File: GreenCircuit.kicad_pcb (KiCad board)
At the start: 2 copper layers, 114.9 x 97.8 mm, 71 parts, among them J1 AVR ISP 6, J2 USB_A-Connector, SW1 SW_Push, SW10 SW_Push, SW11 SW_Push, SW12 SW_Push, SW13 SW_Push, SW14 SW_Push, SW15 SW_Push, SW16 SW_Push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

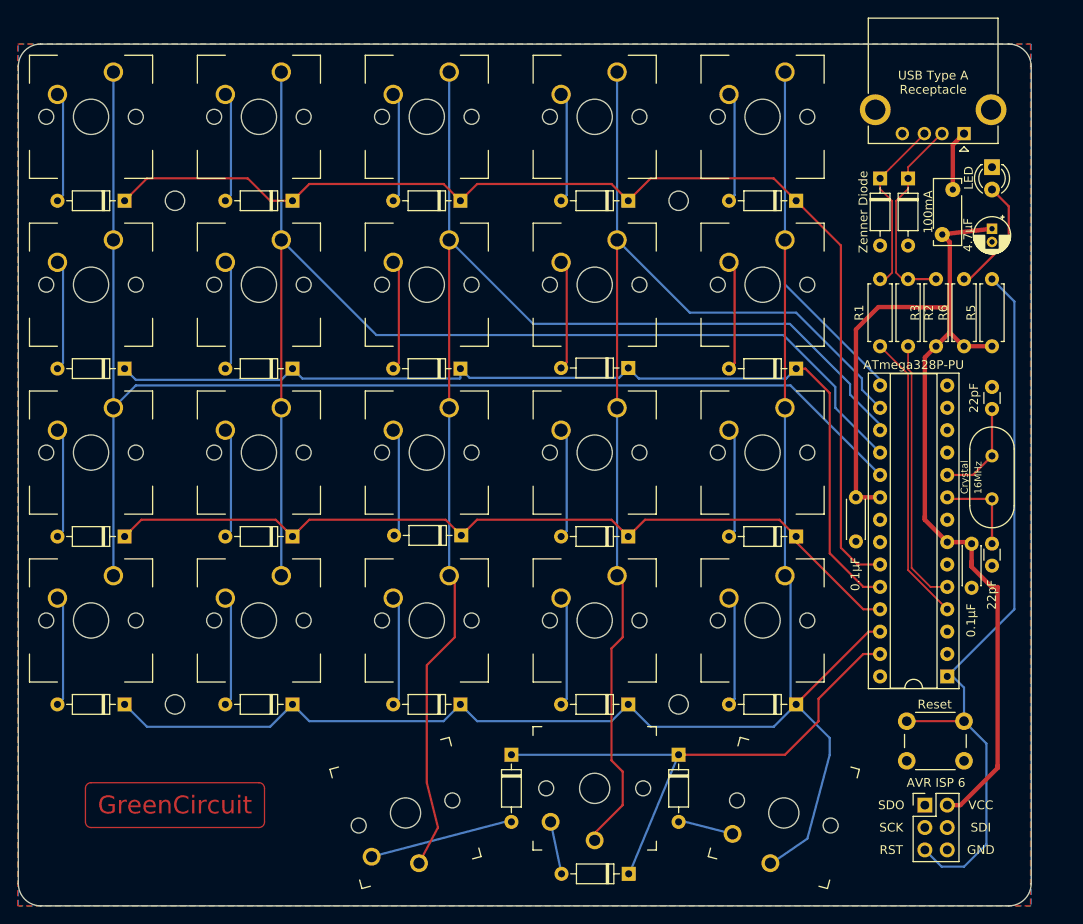
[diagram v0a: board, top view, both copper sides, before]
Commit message: isp reroute
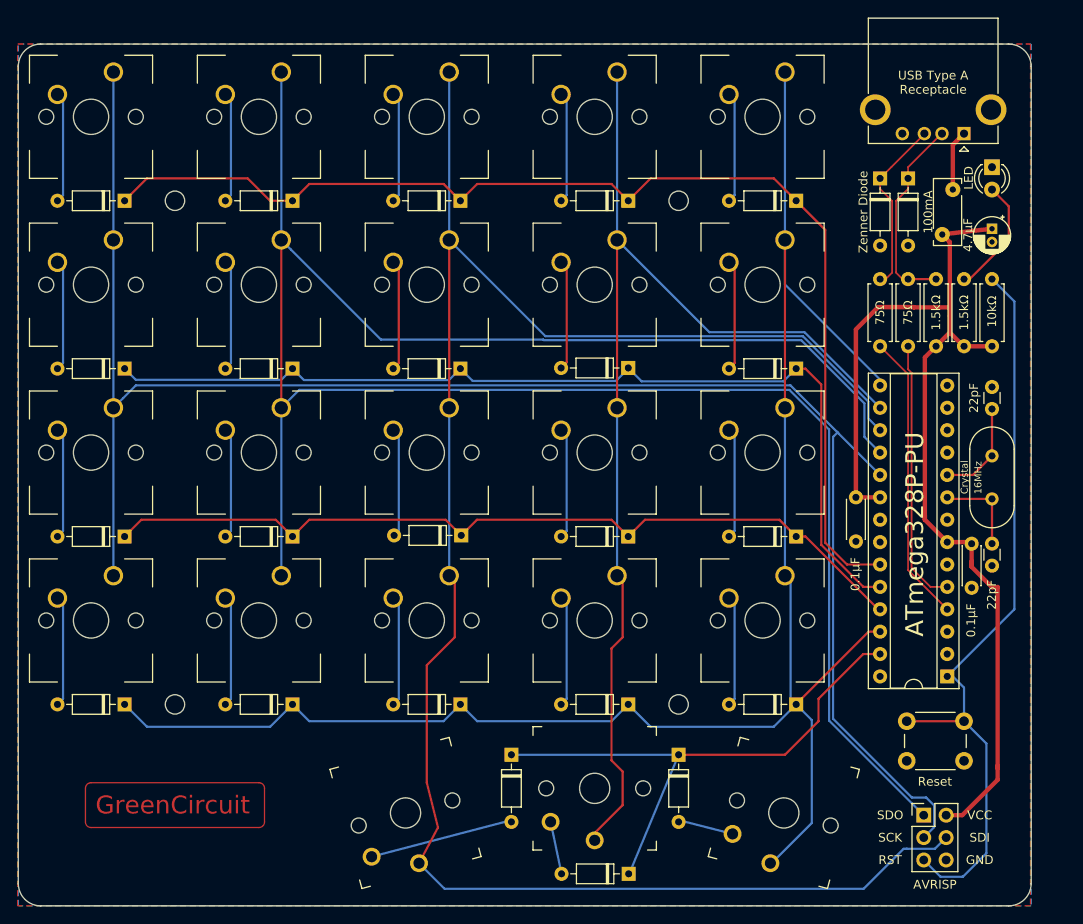
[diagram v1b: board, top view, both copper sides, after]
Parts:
- J1: value AVR ISP 6 -> AVRISP
- moved J1 1.15 mm to (179.8, 145.7)
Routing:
- net Col1: track 137.1 -> 251.0 mm
- net Col2: track 151.1 -> 214.6 mm
- net Col0: track 149.4 -> 201.9 mm
- net Col4: track 211.8 -> 210.4 mm
- net +5V: track 120.9 -> 122.3 mm
- net Reset: track 85.9 -> 87.2 mm
- net Col3: track 128.3 -> 127.5 mm
- net Row0: track 130.3 -> 131.0 mm
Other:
- board text added: "Rev 0.4 Oct 2020 James Sa"
- board text removed: "Rev 0.3 Sep 2020 James Sa"

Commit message: add indicative LED
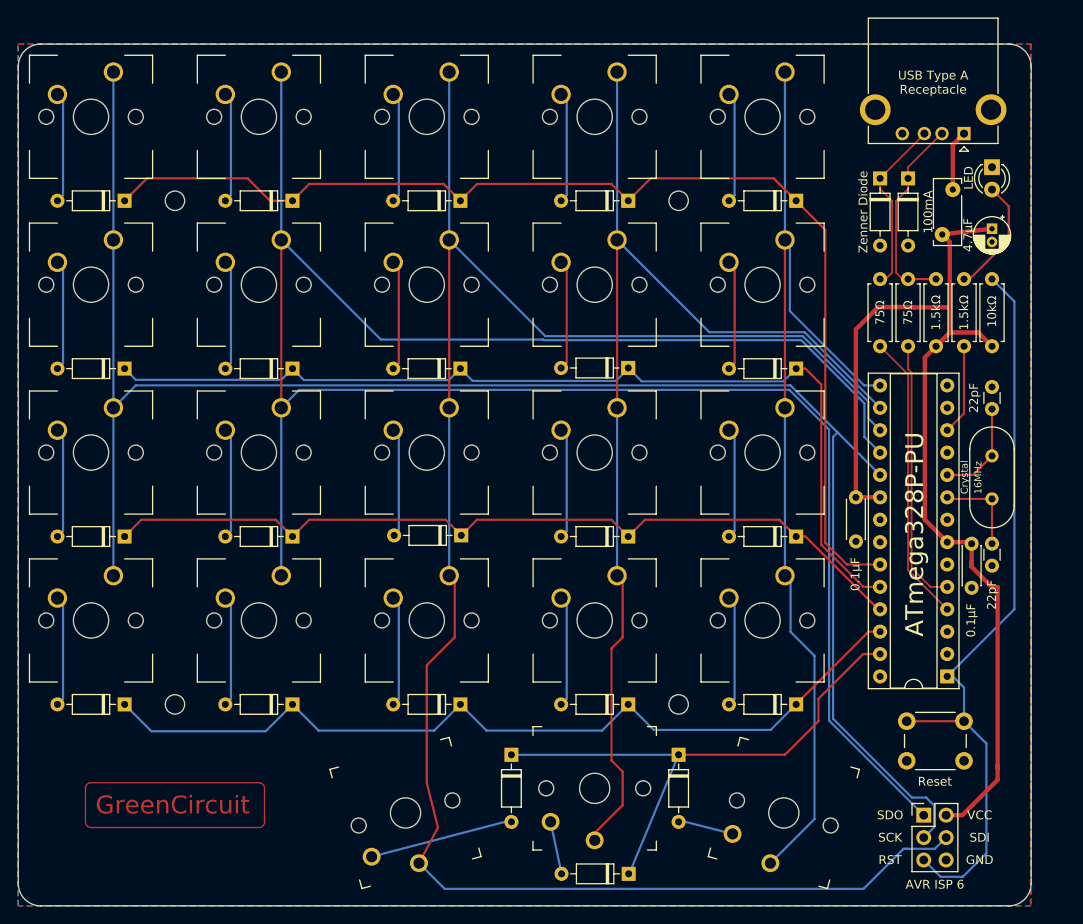
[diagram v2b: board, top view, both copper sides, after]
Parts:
- J1: value AVRISP -> AVR ISP 6
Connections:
- D16 pad 1: Col4 -> Row3
- D17 pad 1: Col4 -> Row3
- D18 pad 1: Col4 -> Row3
- D19 pad 1: Col4 -> Row3
- D20 pad 1: Col4 -> Row3
- R6 pad 1: +5V -> Net-(R6-Pad1)
- U1 pad 12: (no net) -> Net-(R6-Pad1)
- U1 pad 26: Col4 -> Row3
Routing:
- net Row3: track 0.00 -> 99.0 mm
- net Col4: track 210.4 -> 115.5 mm
- net Net-(R6-Pad1): track 0.00 -> 10.4 mm

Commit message: 220ohm for LED
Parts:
- R6: value 1.5kΩ -> 220Ω
- moved R5 3.17 mm to (184.4, 92.5)
- moved R6 3.17 mm to (187.5, 92.5)
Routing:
- net +5V: track 122.3 -> 119.1 mm
- net Net-(R6-Pad1): track 10.4 -> 11.6 mm
- net Net-(D26-Pad2): track 13.4 -> 12.3 mm
- net Reset: track 87.2 -> 88.1 mm

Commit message: v0.5
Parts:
- removed the J2 at (184.4, 68.4)
- removed Logo_KiCad: KiCad-Logo_20mm_SilkScreen, Symbol:KiCad-Logo_20mm_SilkScreen
- removed OSHW_Logo: OSHW-Logo2_36.5x30mm_SilkScreen, Symbol:OSHW-Logo2_36.5x30mm_SilkScreen
- added Mini USB: USB_B_Mini, digikey-footprints:USB_Mini_B_Female_548190519, F.Cu at (182.5, 66.5)
- J2: renamed from J1; value AVR ISP 6 -> AVR ISP
- moved D23 32.1 mm to (183.6, 144.2), turned to 255 degrees
- moved D22 20.3 mm to (161.5, 138.9), turned to 270 degrees
- moved H3 19.1 mm to (94.8, 114.1)
- moved D18 14.5 mm to (132.9, 119.8), turned to 270 degrees
- moved D3 14.5 mm to (132.9, 62.7), turned to 270 degrees
- moved D8 14.5 mm to (132.9, 81.7), turned to 270 degrees
- moved D1 14.5 mm to (94.8, 62.7), turned to 270 degrees
- moved D10 14.5 mm to (171.0, 81.7), turned to 270 degrees
- moved D16 14.5 mm to (94.8, 119.8), turned to 270 degrees
- moved D17 14.5 mm to (113.9, 119.8), turned to 270 degrees
- moved D19 14.5 mm to (152.0, 119.8), turned to 270 degrees
- moved D2 14.5 mm to (113.9, 62.7), turned to 270 degrees
- moved D20 14.5 mm to (171.0, 119.8), turned to 270 degrees
- moved D4 14.5 mm to (152.0, 62.7), turned to 270 degrees
- moved D5 14.5 mm to (171.0, 62.7), turned to 270 degrees
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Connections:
- U1 pad 3: (no net) -> D-
- U1 pad 5: D- -> (no net)
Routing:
- net Col1: track 251.0 -> 185.6 mm
- net Col2: track 214.6 -> 186.1 mm
- net Row1: track 111.2 -> 136.6 mm
- net Row2: track 95.4 -> 118.5 mm
- net Row0: track 131.0 -> 154.0 mm
- net Row4: track 62.7 -> 48.0 mm
- net Col4: track 115.5 -> 100.8 mm
- net Reset: track 88.1 -> 75.0 mm
- net Col3: track 127.5 -> 115.0 mm
- net Row3: track 99.0 -> 87.3 mm
- net Net-(D21-Pad2): track 16.4 -> 9.01 mm
- net +5V: track 119.1 -> 112.4 mm
- net Net-(D19-Pad2): track 12.6 -> 6.24 mm
- net Net-(D4-Pad2): track 12.6 -> 6.24 mm
- net Net-(D14-Pad2): track 12.6 -> 6.24 mm
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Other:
- board size 114.9 x 97.8 mm -> 118.1 x 97.2 mm
- board text added: "Rev 0.5 Oct 2020 James Sa"
- board text removed: "Design with"
- board text removed: "Rev 0.4 Oct 2020 James Sa"
- board text removed: "USB Type A Receptacle"

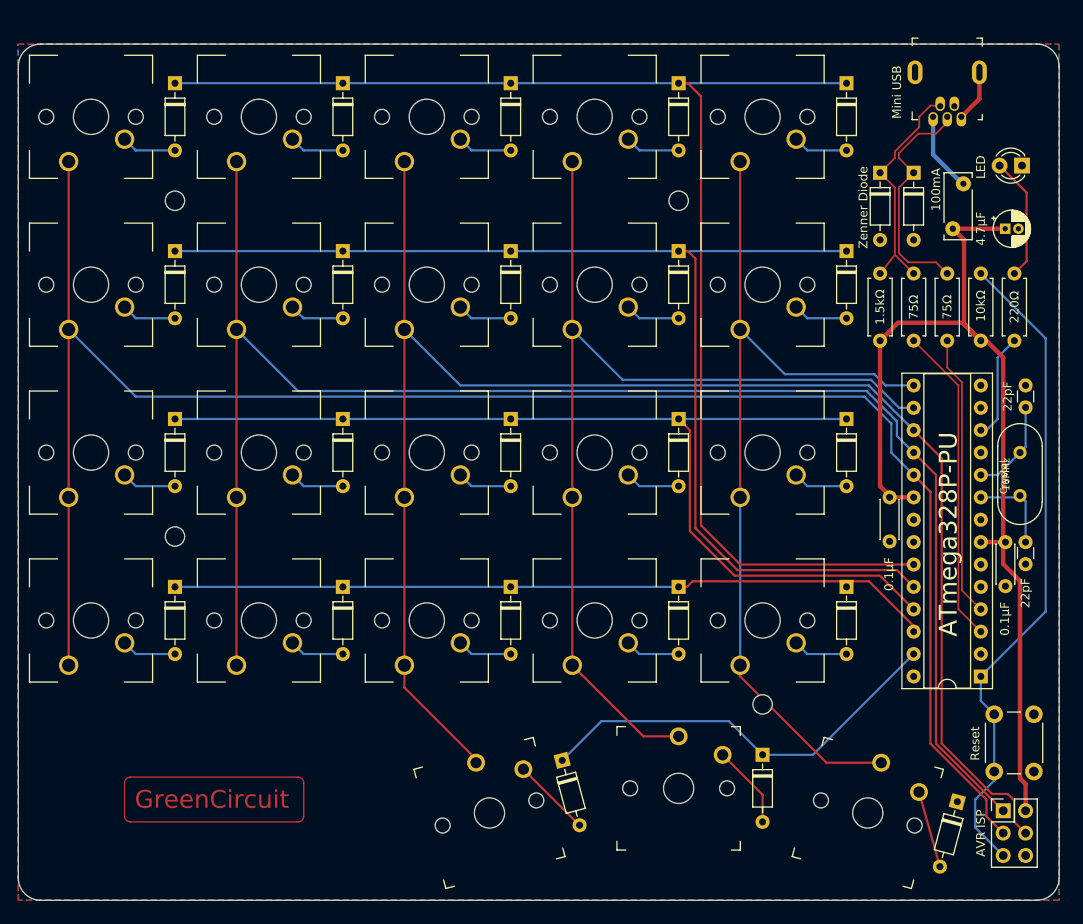
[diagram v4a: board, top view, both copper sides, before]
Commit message: new pcb size with M3 screw for buttom acrylic
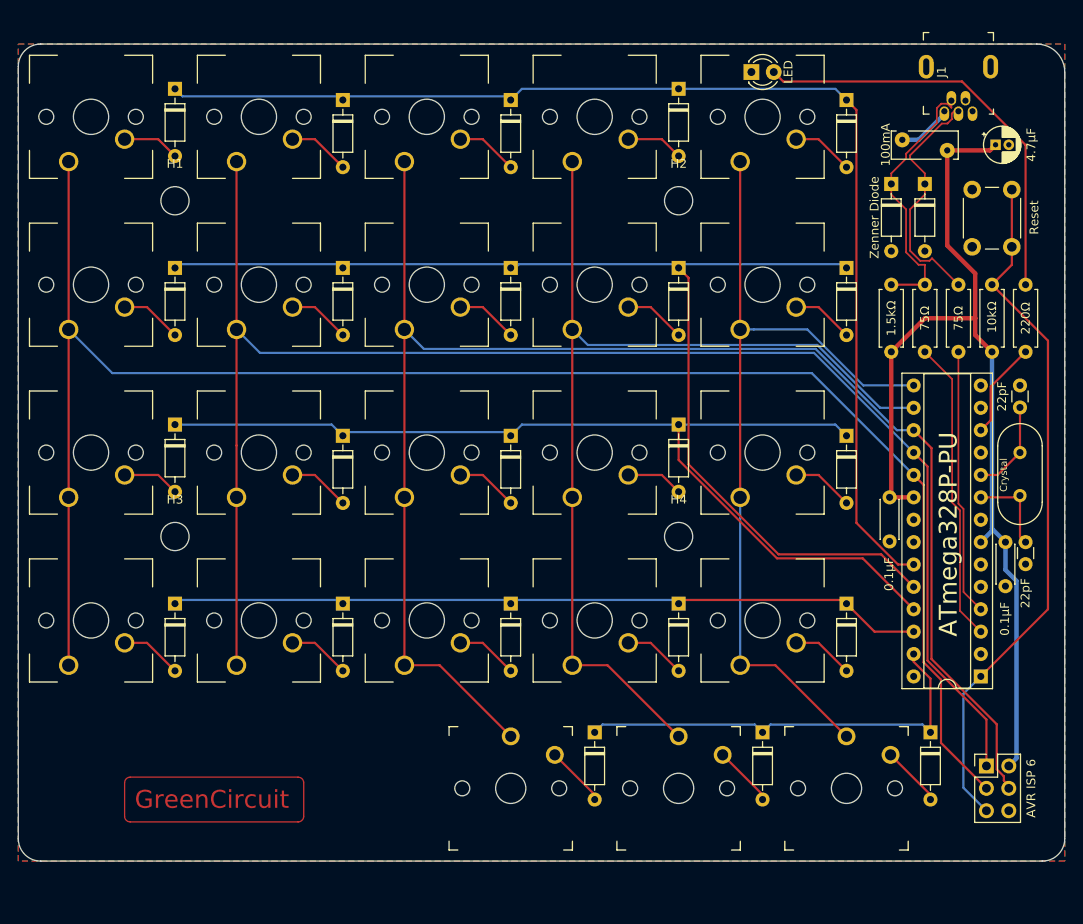
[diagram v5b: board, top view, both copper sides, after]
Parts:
- H1, H2, H3, H4: footprint MountingHole:MountingHole_2.2mm_M2 -> MountingHole:MountingHole_3.2mm_M3
- J1: renamed from Mini USB
- J2: value AVR ISP -> AVR ISP 6
- moved Reset1 66.1 mm to (189.8, 74.8), turned to 270 degrees
- moved D26 32.5 mm to (160.2, 61.4), turned to 0 degrees
- moved H4 21.3 mm to (152.0, 114.1)
- moved C3 9.59 mm to (187.9, 69.7)
- moved F1 8.91 mm to (182.5, 70.3), turned to 180 degrees
- moved D23 8.44 mm to (180.6, 136.3), turned to 270 degrees
- moved J2 5.43 mm to (186.9, 140.2)
- moved D21 4.86 mm to (142.4, 136.3), turned to 270 degrees
- moved SW21 3.69 mm to (132.9, 142.7), turned to 180 degrees
- moved SW23 3.69 mm to (171.0, 142.7), turned to 180 degrees
- moved D22 2.54 mm to (161.5, 136.3)
- moved D10 1.91 mm to (171.0, 83.6)
- moved D16 1.91 mm to (94.8, 121.7)
- moved D17 1.91 mm to (113.9, 121.7)
- moved D18 1.91 mm to (132.9, 121.7)
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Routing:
- net Net-(D26-Pad2): track 14.1 -> 47.9 mm
- net Row0: track 154.0 -> 135.0 mm
- net Col0: track 206.7 -> 198.9 mm
- net Col1: track 185.6 -> 178.8 mm
- net Col2: track 186.1 -> 180.2 mm
- net Col4: track 100.8 -> 94.9 mm
- net GND: track 5.90 -> 0.00 mm
- net Row1: track 136.6 -> 131.6 mm
- net Reset: track 75.0 -> 79.1 mm
- net /DN: track 26.7 -> 30.8 mm
- net Net-(F1-Pad2): track 9.02 -> 6.31 mm
- net Net-(D21-Pad2): track 9.01 -> 6.40 mm
- net Net-(D22-Pad2): track 9.48 -> 6.94 mm
- net Net-(D23-Pad2): track 8.79 -> 6.94 mm
- net Row2: track 118.5 -> 116.7 mm
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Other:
- board size 118.1 x 97.2 mm -> 118.7 x 92.7 mm
- board text added: "Green Circuit Rev 0.5 Oct 2020 James Sa"
- board text added: "“People who are really serious about software should make their own hardware” Alan Kay"
- board text removed: "Rev 0.5 Oct 2020 James Sa"

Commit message: v.6
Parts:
- added G***: LOGO, footprints:logo, B.Cu at (128.5, 104.6)
- J2: value AVR ISP 6 -> ISP
- moved J2 2.53 mm to (186.9, 137.6)
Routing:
- net Row2: track 116.7 -> 101.5 mm
- net Row1: track 131.6 -> 118.8 mm
- net GND: track 0.00 -> 6.19 mm
- net Col0: track 198.9 -> 196.3 mm
- net Col1: track 178.8 -> 176.2 mm
- net Col2: track 180.2 -> 177.7 mm
- net +5V: track 111.7 -> 109.4 mm
- net Reset: track 79.1 -> 77.3 mm
- net Net-(D26-Pad2): track 47.9 -> 49.0 mm
- net Row0: track 135.0 -> 136.0 mm
- net Row3: track 86.5 -> 87.2 mm
- net Net-(F1-Pad2): track 6.31 -> 7.01 mm
- net Row4: track 49.3 -> 49.9 mm
- net /DP: track 27.5 -> 28.1 mm
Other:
- board text added: "Green Circuit Rev 0.6 Nov 2020 James Sa"
- board text removed: "Green Circuit Rev 0.5 Oct 2020 James Sa"
- board text removed: "“People who are really serious about software should make their own hardware” Alan Kay"
